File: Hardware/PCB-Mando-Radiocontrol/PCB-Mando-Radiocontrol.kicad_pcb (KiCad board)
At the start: 2 copper layers, 132 x 66 mm, 23 parts, among them J2 ALIMENTACION, J3 USB 2.0 a UART TTL 6 pines CP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, SW1 Encendido, U1 ATMEGA328P, U2 Nrf24l01, U3 AMS1117-3.3, U4 AMS1117-5.0, U5 COM-09032, U6 COM-09032, Y1 16MHZ

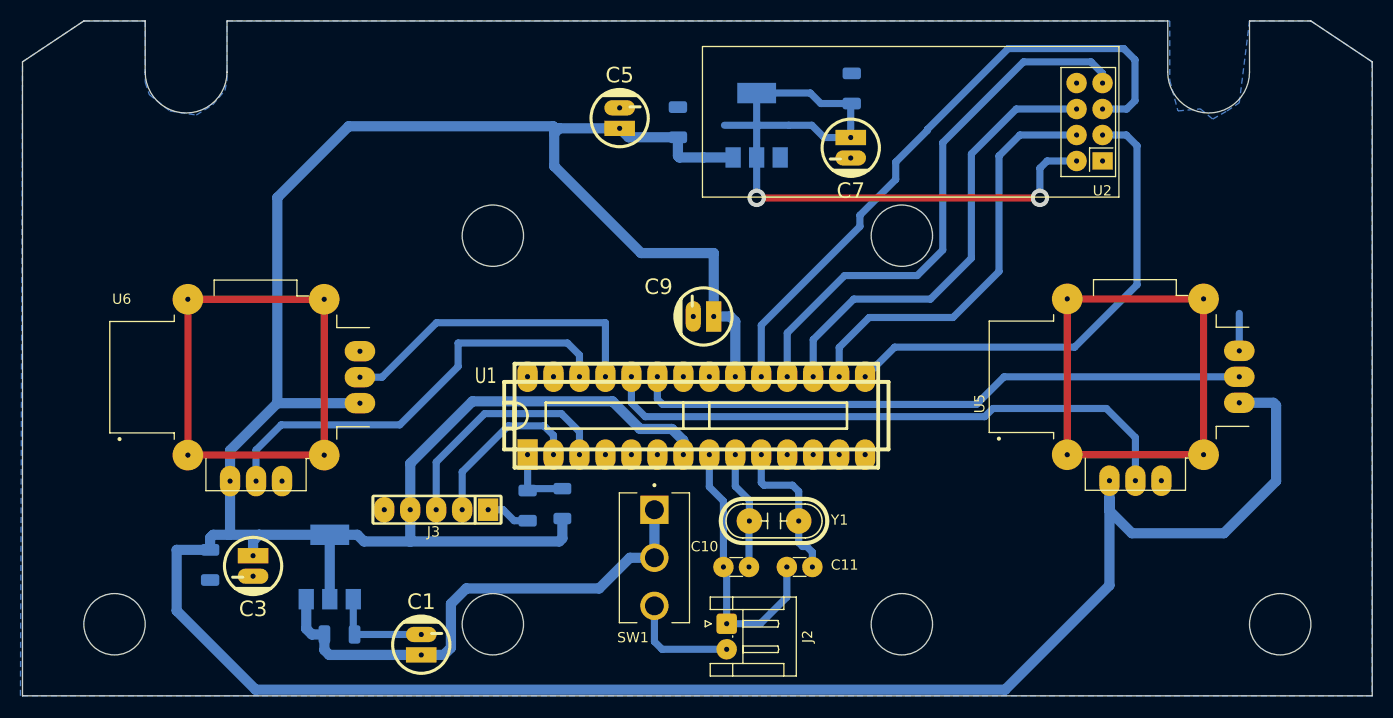
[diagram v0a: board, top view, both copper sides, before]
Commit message: aplique sugerencias de markow y mias, agregue botones modifique esquematico y pcb
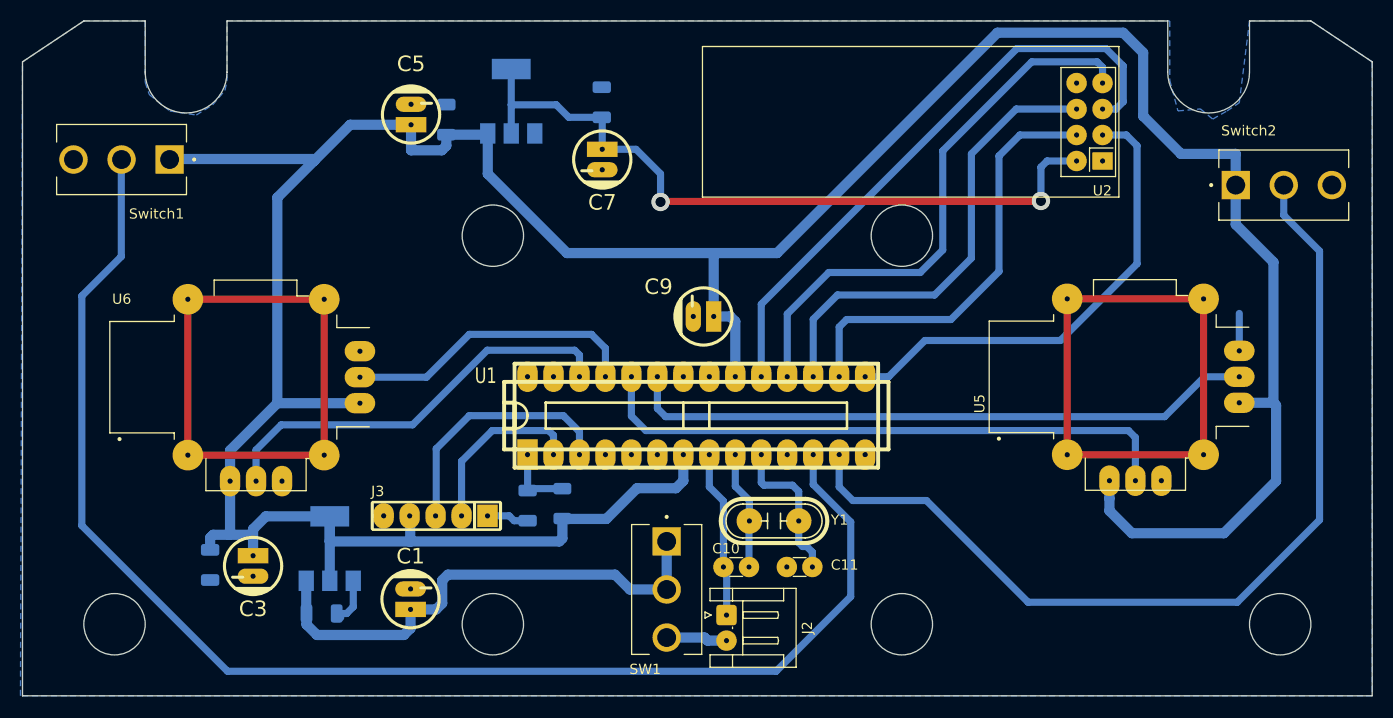
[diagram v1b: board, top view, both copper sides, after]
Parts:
- added Switch1: ~, Footprints:SW_100SP3T1B1M2QE, F.Cu at (100.7, 77.5)
- added Switch2: ~, Footprints:SW_100SP3T1B1M2QE, F.Cu at (214.3, 80.0)
- C2, C4: value 0.1uF -> 100nF
- SW1: value Encendido -> SW_SPDT
- moved C8 24.5 mm to (147.7, 72.0)
- moved C7 24.3 mm to (147.7, 77.5)
- moved U3 24.1 mm to (138.8, 71.8)
- moved C6 22.7 mm to (132.4, 73.7)
- moved C5 20.4 mm to (129.0, 73.2)
- moved C1 4.57 mm to (128.9, 120.5)
- moved SW1 3.32 mm to (154.0, 119.6)
- moved C2 2.70 mm to (120.2, 122.0)
- moved U4 1.80 mm to (121.0, 115.6)
- moved J2 0.85 mm to (159.8, 122.1)
- moved J3 0.60 mm to (131.4, 112.4)
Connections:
- U1 pad 12: unconnected-(U1-D6-Pad12) -> /SwIzq
- U1 pad 13: unconnected-(U1-D7-Pad13) -> /SwDer
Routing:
- net /SwIzq: track 0.00 -> 137.0 mm
- net /SwDer: track 0.00 -> 92.3 mm
- net +5V: track 367.0 -> 323.8 mm
- net GND: track 155.1 -> 139.4 mm
- net /BAT: track 10.9 -> 5.97 mm
- net /SCK: track 62.5 -> 59.4 mm
- net /PotIzqA: track 31.5 -> 29.1 mm
- net /PotIzqB: track 43.0 -> 41.0 mm
- net +3V3: track 70.7 -> 72.5 mm
- net /PotDerA: track 60.4 -> 62.0 mm
- net /TX: track 23.6 -> 24.8 mm
- net /CE: track 47.7 -> 46.5 mm
- net /CSK: track 41.3 -> 42.5 mm
- net /MOSI: track 44.7 -> 45.9 mm
- net /MISO: track 53.7 -> 54.6 mm
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
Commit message: Ordene serigrafia y cambie los capacitores c11 y c12 tht por cmd
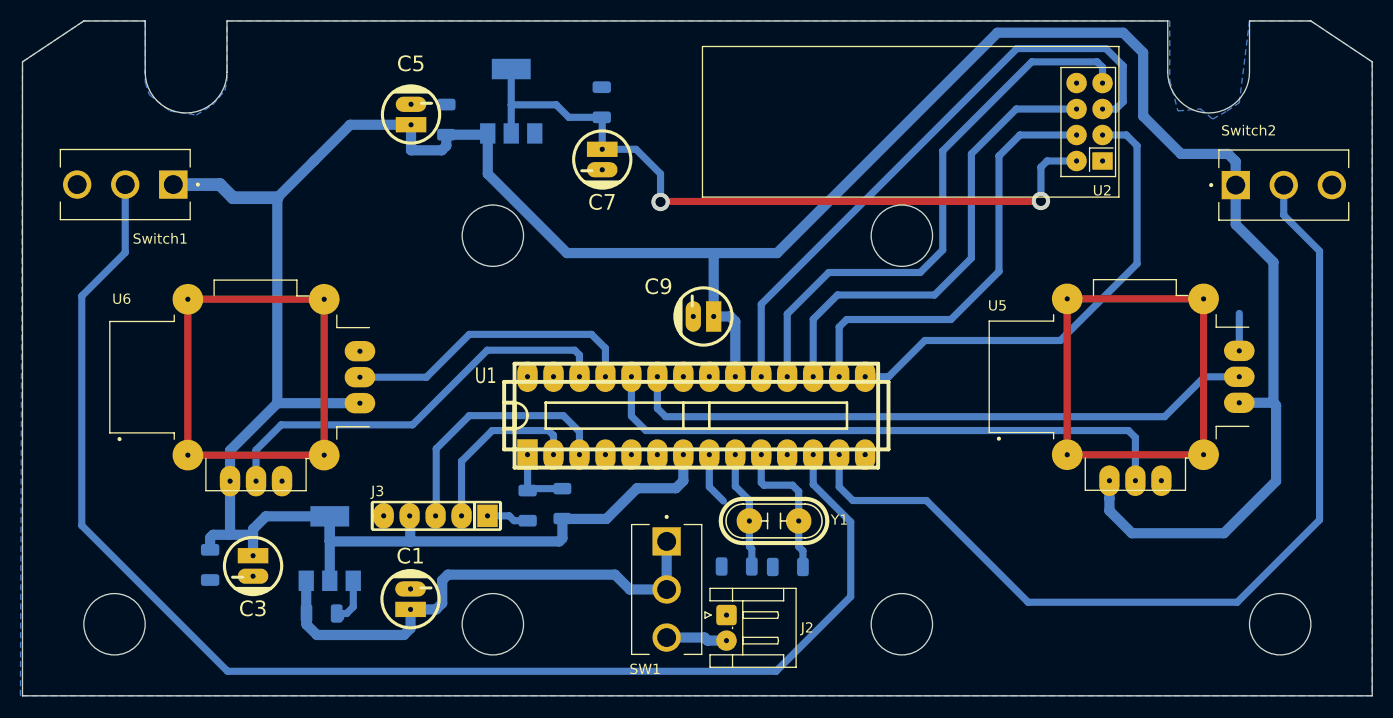
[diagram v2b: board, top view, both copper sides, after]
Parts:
- C10, C11: footprint Capacitor_THT:C_Disc_D3.0mm_W1.6mm_P2.50mm -> Capacitor_SMD:C_1206_3216Metric; moved to B.Cu
- SW1: value SW_SPDT -> ~
- Y1: value 16MHZ -> 16KHZ
- moved Switch1 2.48 mm to (101.0, 80.0)
- moved C10 1.30 mm to (160.8, 117.3)
- moved C11 0.10 mm to (165.8, 117.4)
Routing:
- net GND: track 139.4 -> 128.1 mm
- net +5V: track 323.8 -> 319.8 mm
- net /SwIzq: track 137.0 -> 134.6 mm
- net Net-(C11-Pad2): track 14.9 -> 14.3 mm

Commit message: Agregue LED y BUZZER , pcb listo para montar
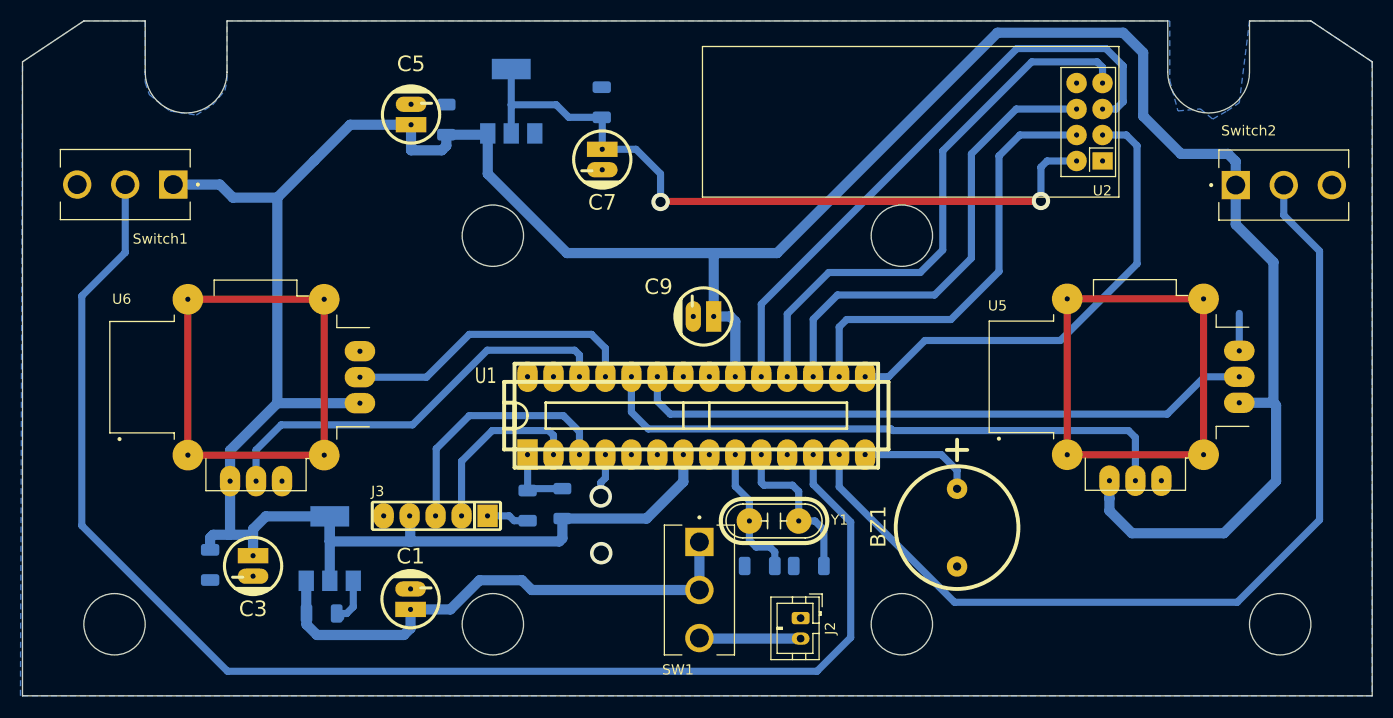
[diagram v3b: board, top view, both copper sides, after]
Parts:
- added BZ1: Buzzer, EESTN5:Buzzer_12mm, F.Cu at (182.4, 113.5)
- J2: footprint Connector_JST:JST_EH_S2B-EH_1x02_P2.50mm_Horizontal -> Connector_JST:JST_PH_B2B-PH-K_1x02_P2.00mm_Vertical
- moved J2 7.26 mm to (167.1, 122.4)
- moved SW1 3.20 mm to (157.2, 119.7)
- moved C10 2.25 mm to (163.1, 117.3)
- moved C11 2.05 mm to (167.9, 117.3)
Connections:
- U1 pad 14: unconnected-(U1-D8-Pad14) -> /BUZZER
- U1 pad 4: unconnected-(U1-D2-Pad4) -> /LED
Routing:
- net /BUZZER: track 0.00 -> 11.4 mm
- net GND: track 128.1 -> 123.0 mm, vias 0 -> 1
- net /LED: track 0.00 -> 4.28 mm, vias 0 -> 1
- net /BAT: track 5.97 -> 9.92 mm
- net /SwIzq: track 134.6 -> 137.0 mm
- net Net-(C11-Pad2): track 14.3 -> 16.0 mm
- net Net-(C10-Pad2): track 11.7 -> 13.3 mm
- net VCC: track 50.1 -> 51.5 mm
- net /PotDerA: track 62.0 -> 61.3 mm

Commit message: aGREGUE LOGO DE bover group srl en B.CU
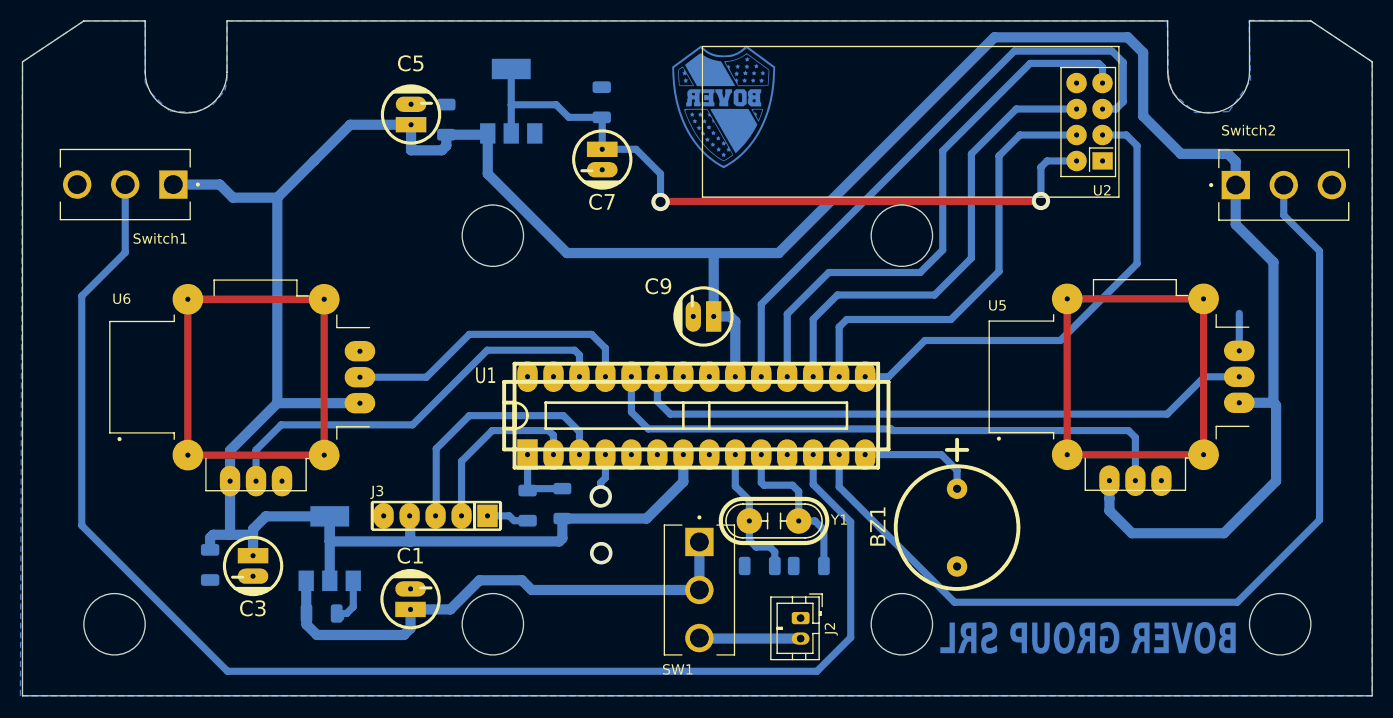
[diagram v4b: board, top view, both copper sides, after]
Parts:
- added G***: LOGO, Footprints:LOGO_BOVER_B.CU, F.Cu at (159.6, 72.4)

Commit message: Agregue serigrafia y ordene
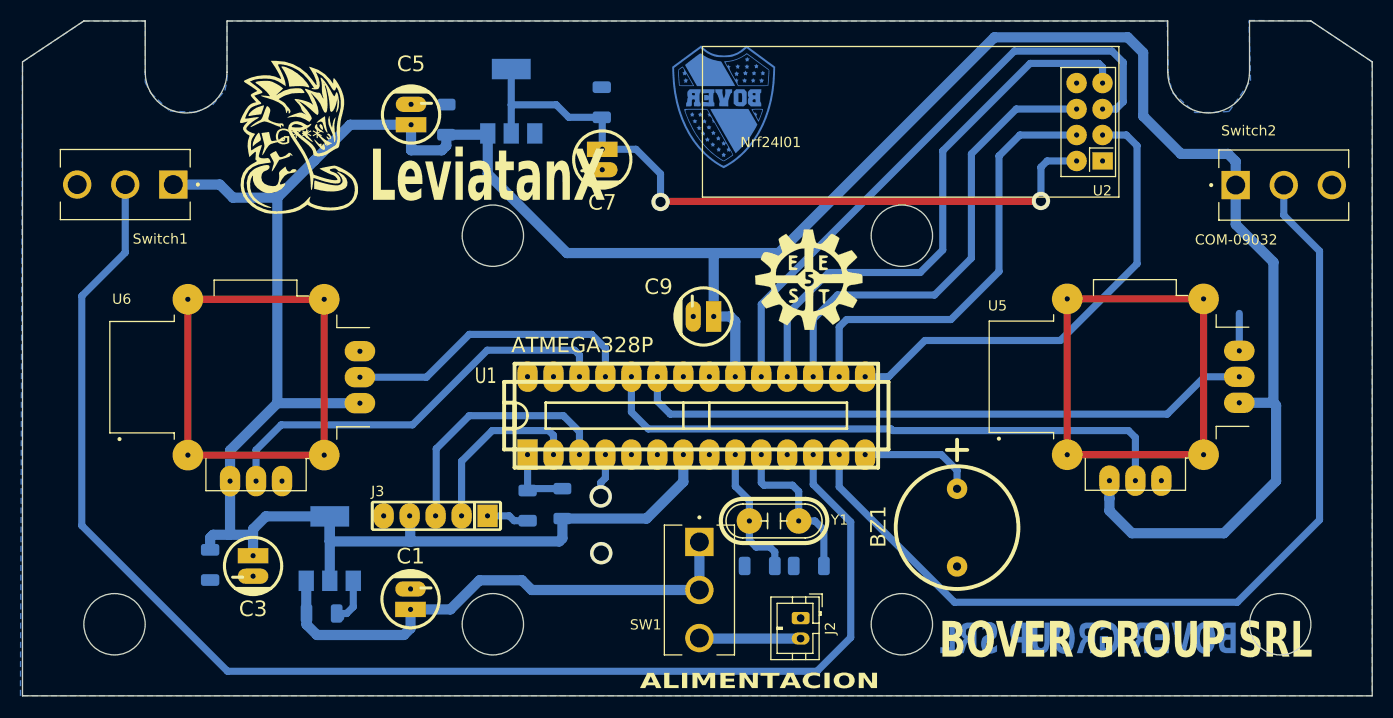
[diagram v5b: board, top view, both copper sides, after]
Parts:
- added G***: LOGO, LOGO, F.Cu at (118.0, 75.3)
- added G***: LOGO, EESTN5:LOGO_EESTN5, F.Cu at (167.9, 89.2)
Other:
- board text added: "BOVER GROUP SRL"
- board text added: "LeviatanX"
